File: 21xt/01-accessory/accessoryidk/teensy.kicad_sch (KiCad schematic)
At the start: 1 part, among them T1 749013011

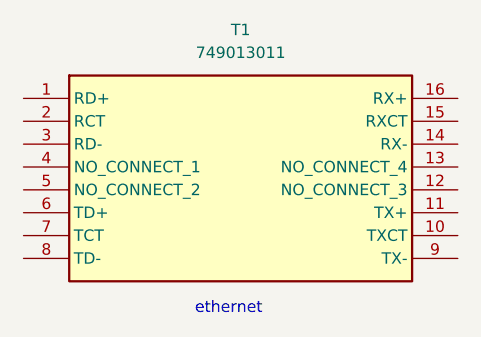
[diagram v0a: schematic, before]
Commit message: Unfinished V1 accessory schematic, remaining teensy connections
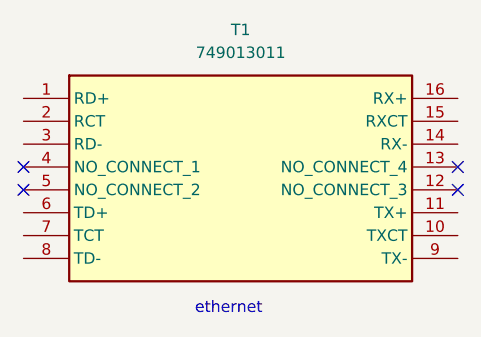
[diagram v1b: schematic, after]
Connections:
- no-connect marks 0 -> 4
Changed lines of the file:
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@@
 (kicad_sch (version 20230121) (generator eeschema)
   (paper "A4")
+  (no_connect (at 194.31 74.93))
+  (no_connect (at 194.31 77.47))
+  (no_connect (at 242.57 74.93))
+  (no_connect (at 242.57 77.47))
   (text "ethernet" (at 213.36 91.44 0)
     (effects (font (size 1.27 1.27)) (justify left bottom))

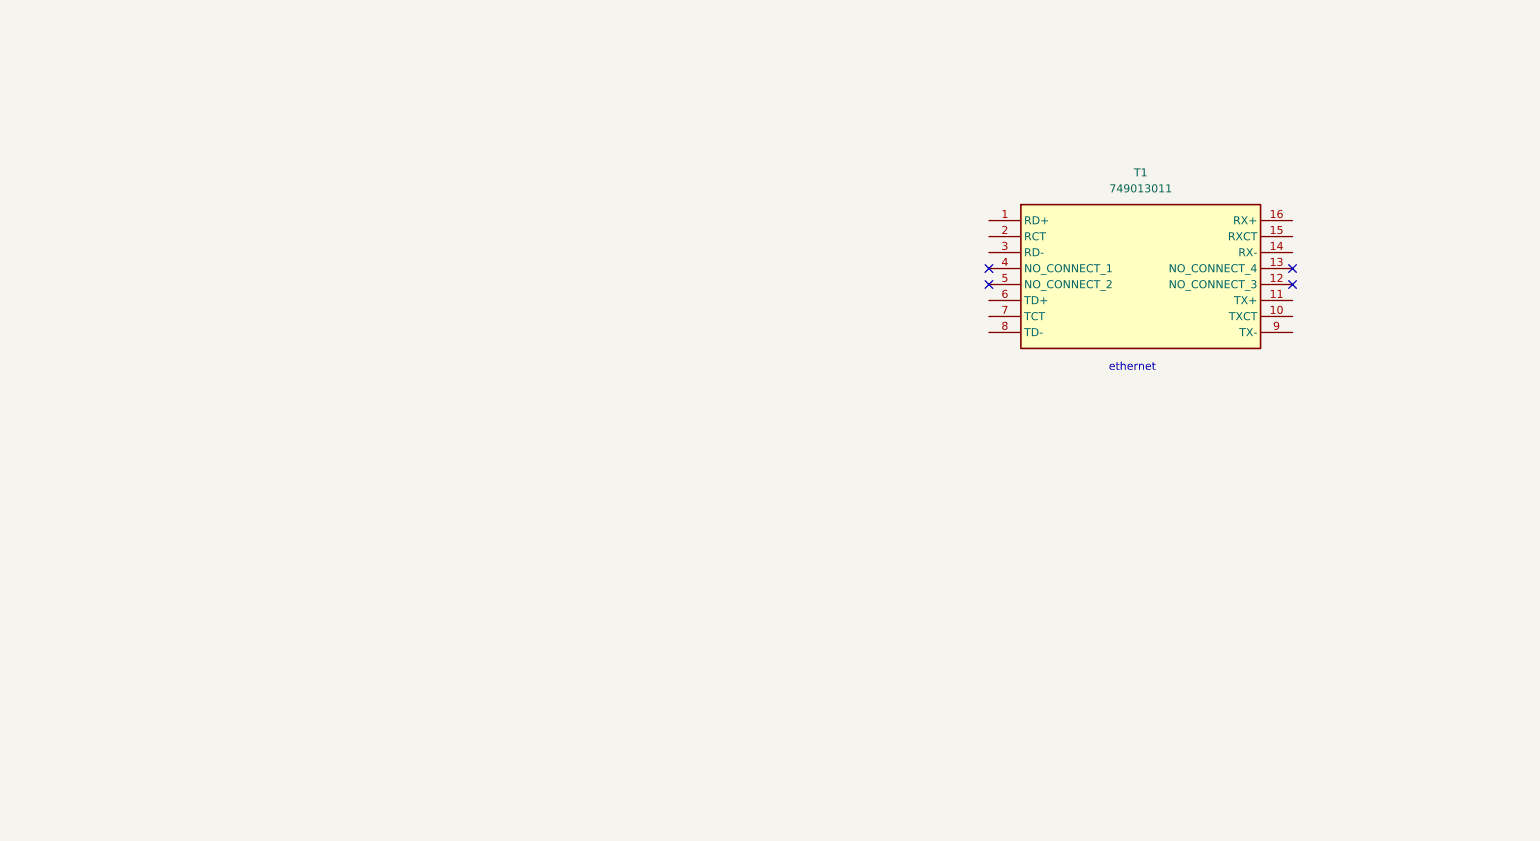
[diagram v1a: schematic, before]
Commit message: Unfinished V1 accessory schematic, adding teensy ADC connections part 1
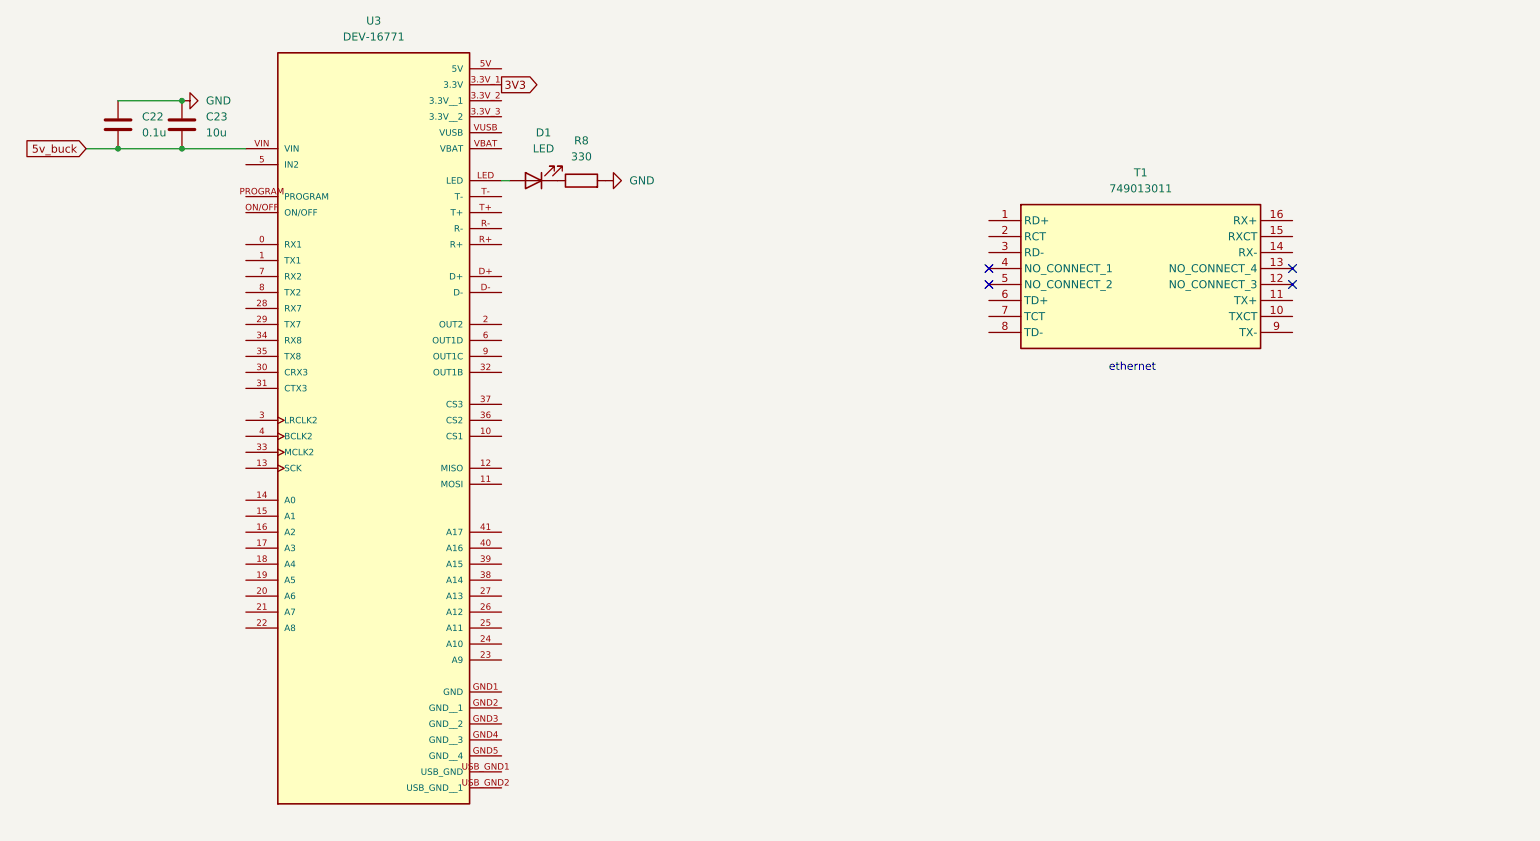
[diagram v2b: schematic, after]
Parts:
- added C22: 0.1u, symbol Device:C
- added C23: 10u, symbol Device:C
- added D1: LED, symbol Device:LED
- added R8: 330, symbol Device:R
- added U3: DEV-16771, mainboxfp:MODULE_DEV-16771, symbol 21xt_symbols:DEV-16771
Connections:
- new net: D1.2 (A), U3.LED
- new net: D1.1 (K), R8.1
- new net 3V3: U3.3.3V_1 (3.3V)
- new net 5v_buck: C22.2, C23.2, U3.VIN
- new net GND: C22.1, C23.1, R8.2

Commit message: Finished V1 schematic, adding footprints
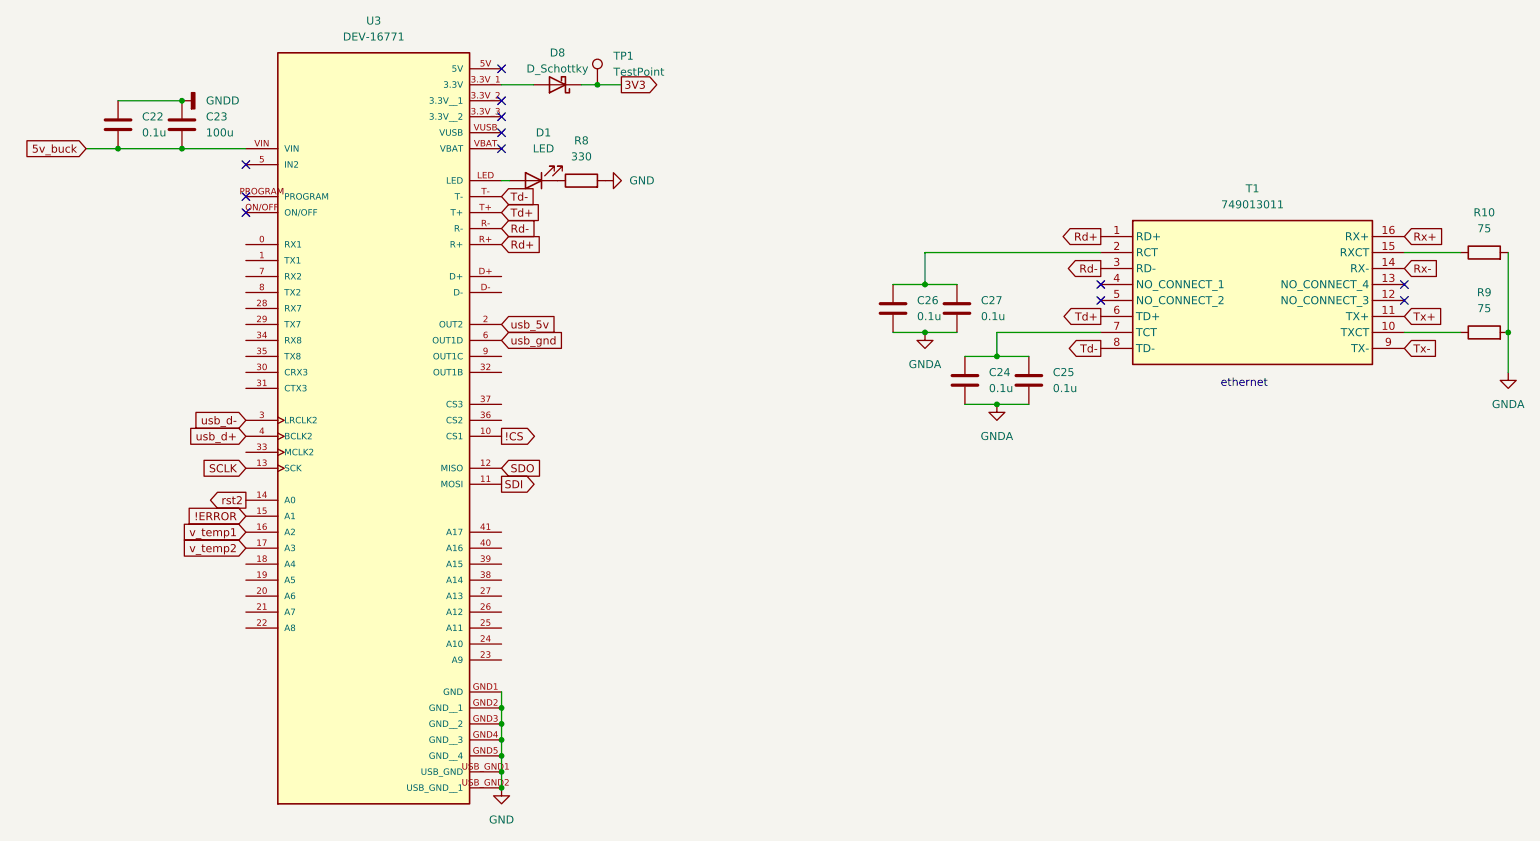
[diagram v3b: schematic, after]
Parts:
- added C24, C25, C26, C27: 0.1u, Capacitor_SMD:C_0603_1608Metric, symbol Device:C
- added D8: D_Schottky, Diode_SMD:D_0603_1608Metric, symbol Device:D_Schottky
- added R10, R9: 75, Resistor_SMD:R_0603_1608Metric, symbol Device:R
- added TP1: TestPoint, TestPoint:TestPoint_Pad_2.0x2.0mm, symbol Connector:TestPoint
- C22: footprint (none) -> Capacitor_SMD:C_0603_1608Metric
- C23: value 10u -> 100u; footprint (none) -> Capacitor_SMD:C_1206_3216Metric
- D1: footprint (none) -> Capacitor_SMD:C_1206_3216Metric
- R8: footprint (none) -> Resistor_SMD:R_0603_1608Metric
- T1: footprint 749013011 -> TestPoint:TestPoint_Pad_2.0x2.0mm
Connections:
- net 3V3: now also D8.1 (K), TP1.1; no longer U3.3.3V_1 (3.3V)
- net GND: now also U3.GND1 (GND), U3.GND2 (GND__1), U3.GND3 (GND__2), U3.GND4 (GND__3), U3.GND5 (GND__4), U3.USB_GND1 (USB_GND), U3.USB_GND2 (USB_GND__1); no longer C22.1, C23.1
- net Rd+: now reaches T1.1 (RD+)
- net Rd+: now also U3.R+
- net at T1.10 (TXCT): now also R9.1
- net Tx+: now reaches T1.11 (TX+)
- net Rx-: now reaches T1.14 (RX-)
- net at T1.15 (RXCT): now also R10.1
- net Rx+: now reaches T1.16 (RX+)
- net at T1.2 (RCT): now also C26.1, C27.1
- net Rd-: now reaches T1.3 (RD-)
- net Rd-: now also U3.R-
- net Td+: now reaches T1.6 (TD+)
- net Td+: now also U3.T+
- net at T1.7 (TCT): now also C24.1, C25.1
- net Td-: now reaches T1.8 (TD-)
- net Td-: now also U3.T-
- net Tx-: now reaches T1.9 (TX-)
- net !CS: now reaches U3.10 (CS1)
- net SDI: now reaches U3.11 (MOSI)
- net SDO: now reaches U3.12 (MISO)
- net SCLK: now reaches U3.13 (SCK)
- net rst2: now reaches U3.14 (A0)
- net !ERROR: now reaches U3.15 (A1)
- net v_temp1: now reaches U3.16 (A2)
- net v_temp2: now reaches U3.17 (A3)
- net usb_5v: now reaches U3.2 (OUT2)
- net usb_d-: now reaches U3.3 (LRCLK2)
- net usb_d+: now reaches U3.4 (BCLK2)
- net usb_gnd: now reaches U3.6 (OUT1D)
- new net: D8.2 (A), U3.3.3V_1 (3.3V)
- new net GNDA: C24.2, C25.2, C26.2, C27.2, R10.2, R9.2
- new net GNDD: C22.1, C23.1
- no-connect marks 4 -> 12
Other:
- moved on the sheet: T1

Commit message: Accessory V1 unfinished layout
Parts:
- T1: footprint TestPoint:TestPoint_Pad_2.0x2.0mm -> 21xt_footprints:749013011
- U3: footprint mainboxfp:MODULE_DEV-16771 -> 21xt_footprints:MODULE_DEV-16771
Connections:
- net GND is gone; now on net GNDA: R8.2, U3.GND1 (GND), U3.GND2 (GND__1), U3.GND3 (GND__2), U3.GND4 (GND__3), U3.GND5 (GND__4), U3.USB_GND1 (USB_GND), U3.USB_GND2 (USB_GND__1)
- net hallfx1_3v3: now reaches U3.18 (A4)
- net hallfx2_3v3: now reaches U3.19 (A5)
- net GNDD renamed Earth
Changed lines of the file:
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@@
   (junction (at 184.15 85.09) (diameter 0) (color 0 0 0 0)
   )
+  (junction (at 195.58 96.52) (diameter 0) (color 0 0 0 0)
+  )
+  (junction (at 55.88 55.88) (diameter 0) (color 0 0 0 0)
+  )
+  (junction (at 195.58 88.9) (diameter 0) (color 0 0 0 0)
+  )
   (junction (at 116.84 157.48) (diameter 0) (color 0 0 0 0)
   )
-  (junction (at 195.58 96.52) (diameter 0) (color 0 0 0 0)
-  )
-  (junction (at 55.88 55.88) (diameter 0) (color 0 0 0 0)
-  )
-  (junction (at 195.58 88.9) (diameter 0) (color 0 0 0 0)
-  )
   (junction (at 116.84 144.78) (diameter 0) (color 0 0 0 0)
   )
   (junction (at 116.84 154.94) (diameter 0) (color 0 0 0 0)
   )
-  (junction (at 66.04 48.26) (diameter 0) (color 0 0 0 0)
+  (junction (at 60.96 48.26) (diameter 0) (color 0 0 0 0)
   )
   (junction (at 276.86 85.09) (diameter 0) (color 0 0 0 0)
@@
     (stroke (width 0) (type default))
   )
-  (wire (pts (xy 55.88 48.26) (xy 66.04 48.26))
+  (wire (pts (xy 55.88 48.26) (xy 60.96 48.26))
     (stroke (width 0) (type default))
   )
   (wire (pts (xy 116.84 147.32) (xy 116.84 149.86))
+    (stroke (width 0) (type default))
+  )
+  (wire (pts (xy 60.96 48.26) (xy 66.04 48.26))
     (stroke (width 0) (type default))
   )
@@
     (effects (font (size 1.27 1.27)) (justify left bottom))
   )
+  (global_label "hallfx1_3v3" (shape input) (at 76.2 121.92 180) (fields_autoplaced)
+    (effects (font (size 1.27 1.27)) (justify right))
+    (property "Intersheetrefs" "${INTERSHEET_REFS}" (at 62.2689 121.92 0)
+      (effects (font (size 1.27 1.27)) (justify right) hide)
+    )
+  )
   (global_label "usb_5v" (shape input) (at 116.84 83.82 0) (fields_autoplaced)
     (effects (font (size 1.27 1.27)) (justify left))
@@
     )
   )
+  (global_label "hallfx2_3v3" (shape input) (at 76.2 124.46 180) (fields_autoplaced)
+    (effects (font (size 1.27 1.27)) (justify right))
+    (property "Intersheetrefs" "${INTERSHEET_REFS}" (at 62.2689 124.46 0)
+      (effects (font (size 1.27 1.27)) (justify right) hide)
+    )
+  )
   (global_label "Td-" (shape input) (at 116.84 63.5 0) (fields_autoplaced)
     (effects (font (size 1.27 1.27)) (justify left))
@@
     )
   )
+  (symbol (lib_id "power:Earth") (at 60.96 48.26 180) (unit 1)
+    (in_bom yes) (on_board yes) (dnp no) (fields_autoplaced)
+    (property "Reference" "#PWR029" (at 60.96 41.91 0)
+      (effects (font (size 1.27 1.27)) hide)
+    )
+    (property "Value" "Earth" (at 60.96 44.45 0)
+      (effects (font (size 1.27 1.27)) hide)
+    )
+    (property "Footprint" "" (at 60.96 48.26 0)
+      (effects (font (size 1.27 1.27)) hide)
+    )
+    (property "Datasheet" "~" (at 60.96 48.26 0)
+      (effects (font (size 1.27 1.27)) hide)
+    )
+    (pin "1")
+    (instances
+      (project "accessoryidk"
+        (path "/5dacc41e-ffff-47d3-9300-200c6018c603/632615cf-95a2-44a3-ae6d-1166f38afe7f"
+          (reference "#PWR029") (unit 1)
+        )
+      )
+    )
+  )
   (symbol (lib_id "Device:R") (at 273.05 85.09 90) (unit 1)
     (in_bom yes) (on_board yes) (dnp no) (fields_autoplaced)
@@
         (path "/5dacc41e-ffff-47d3-9300-200c6018c603/632615cf-95a2-44a3-ae6d-1166f38afe7f"
           (reference "R9") (unit 1)
+        )
+      )
+    )
+  )
+  (symbol (lib_id "power:GNDA") (at 133.35 60.96 90) (unit 1)
+    (in_bom yes) (on_board yes) (dnp no) (fields_autoplaced)
+    (property "Reference" "#PWR030" (at 139.7 60.96 0)
+      (effects (font (size 1.27 1.27)) hide)
+    )
+    (property "Value" "GNDA" (at 137.16 60.96 90)
+      (effects (font (size 1.27 1.27)) (justify right))
+    )
+    (property "Footprint" "" (at 133.35 60.96 0)
+      (effects (font (size 1.27 1.27)) hide)
+    )
+    (property "Datasheet" "" (at 133.35 60.96 0)
+      (effects (font (size 1.27 1.27)) hide)
+    )
+    (pin "1")
+    (instances
+      (project "accessoryidk"
+        (path "/5dacc41e-ffff-47d3-9300-200c6018c603/632615cf-95a2-44a3-ae6d-1166f38afe7f"
+          (reference "#PWR030") (unit 1)
         )
       )
@@
     )
   )
+  (symbol (lib_id "power:GNDA") (at 116.84 157.48 0) (unit 1)
+    (in_bom yes) (on_board yes) (dnp no) (fields_autoplaced)
+    (property "Reference" "#PWR014" (at 116.84 163.83 0)
+      (effects (font (size 1.27 1.27)) hide)
+    )
+    (property "Value" "GNDA" (at 116.84 162.56 0)
+      (effects (font (size 1.27 1.27)))
+    )
+    (property "Footprint" "" (at 116.84 157.48 0)
+      (effects (font (size 1.27 1.27)) hide)
+    )
+    (property "Datasheet" "" (at 116.84 157.48 0)
+      (effects (font (size 1.27 1.27)) hide)
+    )
+    (pin "1")
+    (instances
+      (project "accessoryidk"
+        (path "/5dacc41e-ffff-47d3-9300-200c6018c603/632615cf-95a2-44a3-ae6d-1166f38afe7f"
+          (reference "#PWR014") (unit 1)
+        )
+      )
+    )
+  )
   (symbol (lib_id "Device:C") (at 66.04 52.07 0) (unit 1)
     (in_bom yes) (on_board yes) (dnp no) (fields_autoplaced)
@@
       (effects (font (size 1.27 1.27)))
     )
-    (property "Footprint" "TestPoint:TestPoint_Pad_2.0x2.0mm" (at 256.54 164.77 0)
+    (property "Footprint" "21xt_footprints:749013011" (at 256.54 164.77 0)
       (effects (font (size 1.27 1.27)) (justify left top) hide)
     )
@@
     )
   )
-  (symbol (lib_id "power:GNDD") (at 66.04 48.26 90) (unit 1)
-    (in_bom yes) (on_board yes) (dnp no) (fields_autoplaced)
-    (property "Reference" "#PWR034" (at 72.39 48.26 0)
-      (effects (font (size 1.27 1.27)) hide)
-    )
-    (property "Value" "GNDD" (at 69.85 48.26 90)
-      (effects (font (size 1.27 1.27)) (justify right))
-    )
-    (property "Footprint" "" (at 66.04 48.26 0)
-      (effects (font (size 1.27 1.27)) hide)
-    )
-    (property "Datasheet" "" (at 66.04 48.26 0)
-      (effects (font (size 1.27 1.27)) hide)
-    )
-    (pin "1")
-    (instances
-      (project "accessoryidk"
-        (path "/5dacc41e-ffff-47d3-9300-200c6018c603/632615cf-95a2-44a3-ae6d-1166f38afe7f"
-          (reference "#PWR034") (unit 1)
-        )
-      )
-    )
-  )
   (symbol (lib_id "Device:C") (at 200.66 92.71 0) (unit 1)
     (in_bom yes) (on_board yes) (dnp no) (fields_autoplaced)
@@
       (effects (font (size 1.27 1.27)))
     )
-    (property "Footprint" "mainboxfp:MODULE_DEV-16771" (at 96.52 91.44 0)
+    (property "Footprint" "21xt_footprints:MODULE_DEV-16771" (at 96.52 91.44 0)
       (effects (font (size 1.27 1.27)) (justify bottom) hide)
     )
@@
     )
   )
-  (symbol (lib_id "power:GND") (at 116.84 157.48 0) (unit 1)
-    (in_bom yes) (on_board yes) (dnp no) (fields_autoplaced)
-    (property "Reference" "#PWR043" (at 116.84 163.83 0)
-      (effects (font (size 1.27 1.27)) hide)
-    )
-    (property "Value" "GND" (at 116.84 162.56 0)
-      (effects (font (size 1.27 1.27)))
-    )
-    (property "Footprint" "" (at 116.84 157.48 0)
-      (effects (font (size 1.27 1.27)) hide)
-    )
-    (property "Datasheet" "" (at 116.84 157.48 0)
-      (effects (font (size 1.27 1.27)) hide)
-    )
-    (pin "1")
-    (instances
-      (project "accessoryidk"
-        (path "/5dacc41e-ffff-47d3-9300-200c6018c603/632615cf-95a2-44a3-ae6d-1166f38afe7f"
-          (reference "#PWR043") (unit 1)
-        )
-      )
-    )
-  )
   (symbol (lib_id "Device:R") (at 129.54 60.96 90) (unit 1)
     (in_bom yes) (on_board yes) (dnp no) (fields_autoplaced)
@@
         )
       )
-    )
-  )
-  (symbol (lib_id "power:GND") (at 133.35 60.96 90) (unit 1)
-    (in_bom yes) (on_board yes) (dnp no) (fields_autoplaced)
-    (property "Reference" "#PWR036" (at 139.7 60.96 0)
-      (effects (font (size 1.27 1.27)) hide)
-    )
-    (property "Value" "GND" (at 137.16 60.96 90)
-      (effects (font (size 1.27 1.27)) (justify right))
-    )
-    (property "Footprint" "" (at 133.35 60.96 0)
-      (effects (font (size 1.27 1.27)) hide)
-    )
-    (property "Datasheet" "" (at 133.35 60.96 0)
-      (effects (font (size 1.27 1.27)) hide)
-    )
-    (pin "1")
-    (instances
-      (project "accessoryidk"
-        (path "/5dacc41e-ffff-47d3-9300-200c6018c603/632615cf-95a2-44a3-ae6d-1166f38afe7f"
-          (reference "#PWR036") (unit 1)
-        )
-      )
